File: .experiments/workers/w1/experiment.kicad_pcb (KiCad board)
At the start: 2 copper layers, 140 x 90 mm, 39 parts, among them J1 USB_C, J2 Output, J3 Debug, Q1 FS8205A, U1 USBLC6-2SC6, U2 BQ24072, U3 HY2113-KB5B, U4 MT3608, U5 AP2112K-3.3, U6 LN61CN3302MR-G

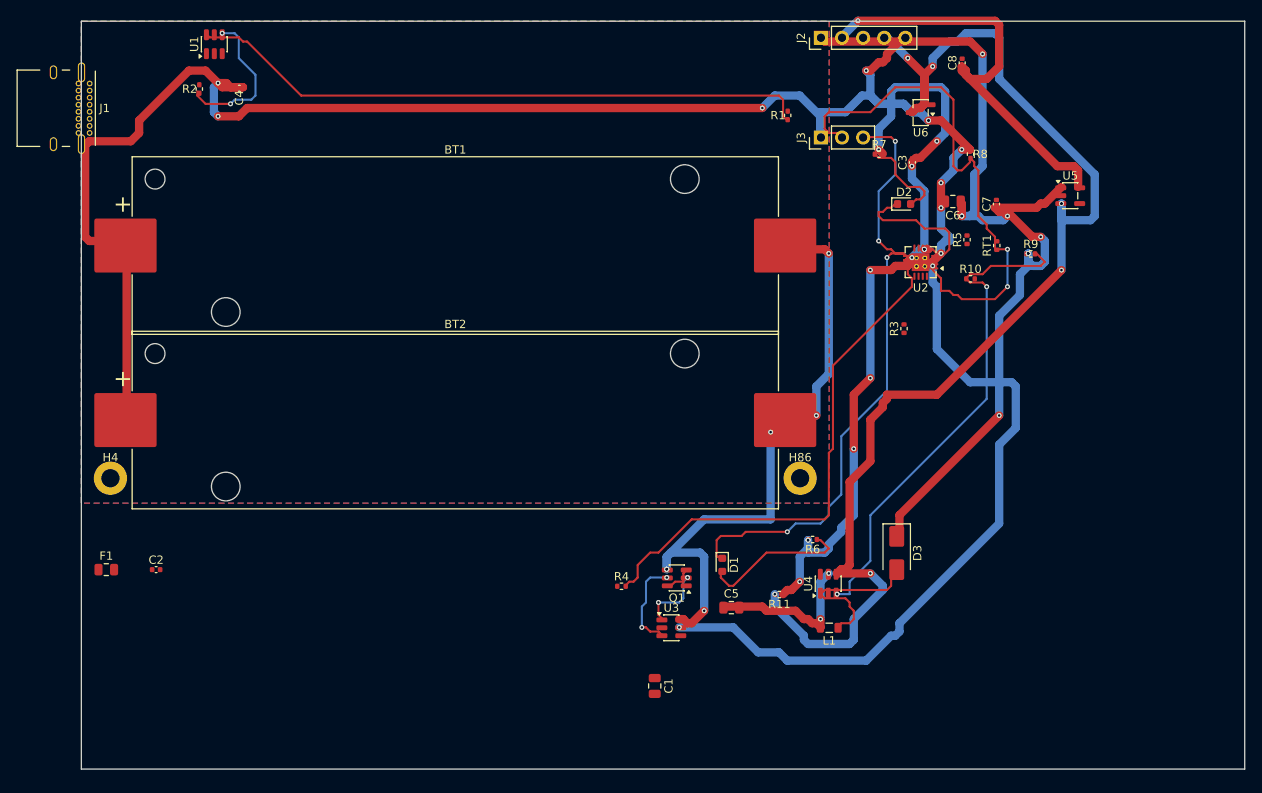
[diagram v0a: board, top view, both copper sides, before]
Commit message: 35-round experiment: best score 25.33, improved routing params
Router and conflict resolution tuning from autonomous optimization loop.
Best config: clearance=0.2051mm, cooling_factor=0.9735, existing_trace_cost=200.0

Co-Authored-By: Claude Opus 4.6 <noreply@anthropic.com>
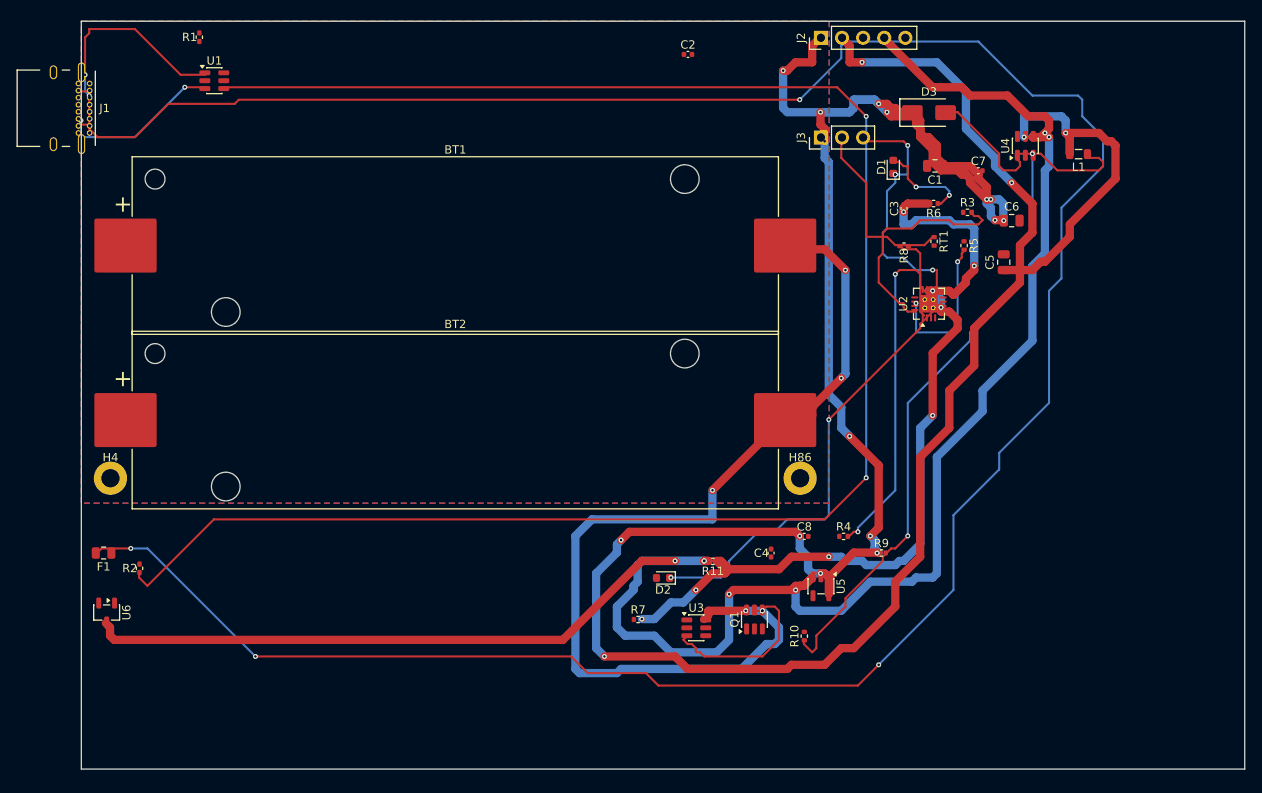
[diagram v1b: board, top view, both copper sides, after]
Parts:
- moved U6 115.0 mm to (3.04, 71.2), turned to -90 degrees
- moved C2 89.1 mm to (73.0, 4.00)
- moved C4 85.0 mm to (83.0, 64.0), turned to 90 degrees
- moved R1 71.4 mm to (14.2, 1.92)
- moved C1 71.1 mm to (102.7, 17.4), turned to 180 degrees
- moved L1 64.4 mm to (120.0, 16.0)
- moved R7 63.1 mm to (67.0, 72.0)
- moved C8 60.1 mm to (87.0, 62.0), turned to 0 degrees
- moved R2 58.1 mm to (7.00, 65.8)
- moved U4 57.8 mm to (113.6, 15.0)
- moved U5 55.8 mm to (89.0, 68.0), turned to -90 degrees
- moved D2 53.5 mm to (70.0, 67.0), turned to 180 degrees
- moved D3 53.1 mm to (102.0, 11.0), turned to 0 degrees
- moved C5 52.9 mm to (111.0, 29.0), turned to 90 degrees
- moved D1 52.1 mm to (97.7, 17.5), turned to 90 degrees
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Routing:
- net Net-(F1-Pad2): track 0.00 -> 317.3 mm, vias 0 -> 4
- net /VBAT: track 293.0 -> 0.00 mm, vias 14 -> 0
- net Net-(R2-Pad1): track 18.4 -> 216.2 mm
- net /3V3: track 52.5 -> 176.8 mm, vias 2 -> 6
- net /EN: track 149.0 -> 238.1 mm, vias 8 -> 6
- net Net-(R1-Pad1): track 75.5 -> 0.00 mm
- net /CHG_N: track 75.4 -> 30.9 mm
- net /CELL_NEG: track 75.5 -> 118.9 mm
- net Net-(D2-K): track 18.7 -> 53.8 mm, vias 0 -> 2
- net /5V: track 115.5 -> 146.3 mm, vias 8 -> 13
- net /NTC_SENSE: track 62.8 -> 32.7 mm, vias 2 -> 0
- net Net-(U2-ISET): track 0.00 -> 27.4 mm
- net Net-(J1-CC1): track 0.00 -> 24.7 mm, vias 0 -> 2
- net /VSYS_BOOST: track 19.4 -> 43.5 mm
- net Net-(U2-ILIM): track 62.7 -> 39.7 mm, vias 0 -> 2
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
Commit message: 45-round experiment: best score 25.66, all nets routed (26/26)
Fixed A* performance by increasing max_search from 100k->500k to handle
high trace costs (100.0) without timing out. Kept high cost + coarse grid
(0.5mm) to prevent shorts while still routing efficiently.

Best config: edge_margin=5.7493mm, cooling_factor=0.9764, existing_trace_cost=200, max_rips=8

Co-Authored-By: Claude Opus 4.6 <noreply@anthropic.com>
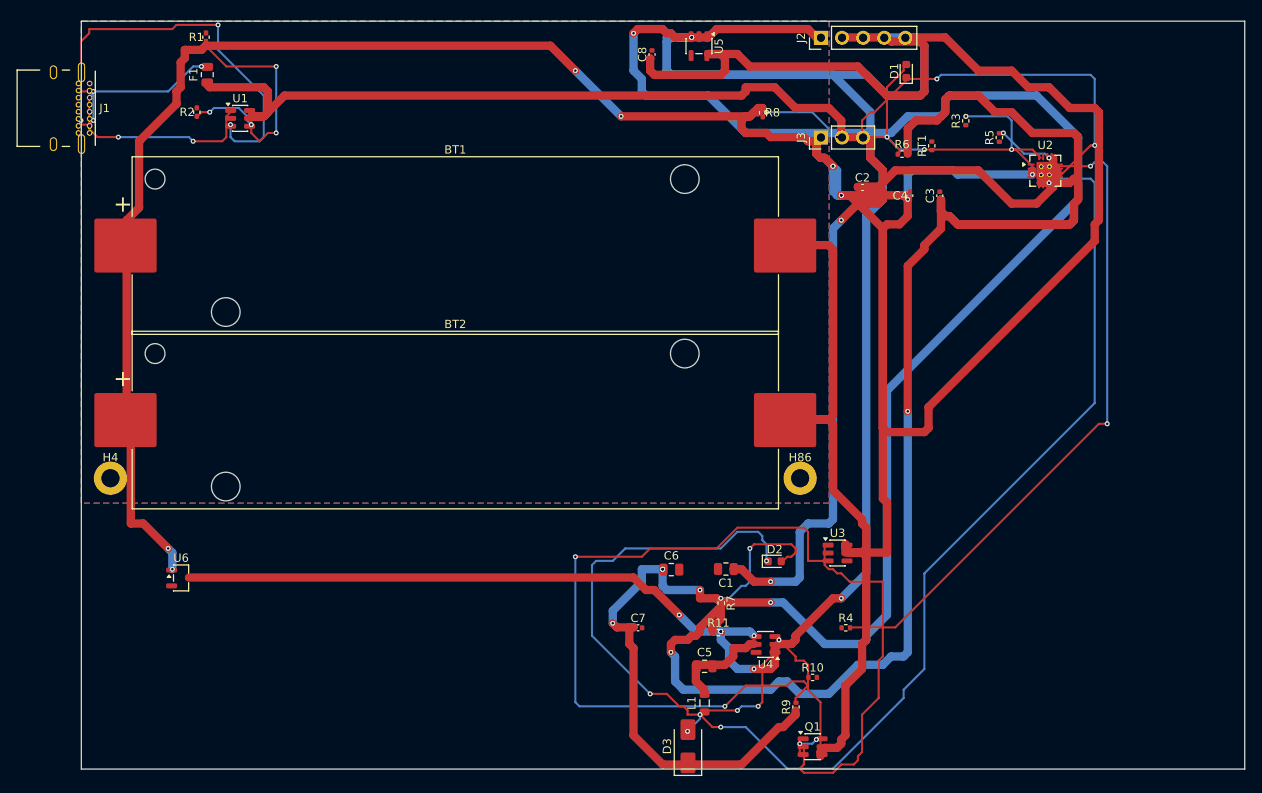
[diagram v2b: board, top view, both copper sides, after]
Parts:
- moved D3 81.6 mm to (73.0, 87.3), turned to 90 degrees
- moved L1 79.9 mm to (75.0, 82.1), turned to 90 degrees
- moved C7 68.6 mm to (67.0, 73.0)
- moved U4 67.7 mm to (82.3, 75.0), turned to 180 degrees
- moved U5 66.6 mm to (74.3, 3.00)
- moved C8 60.8 mm to (68.7, 4.00), turned to 90 degrees
- moved C5 60.5 mm to (75.0, 77.6), turned to 0 degrees
- moved F1 58.9 mm to (15.2, 6.43), turned to 90 degrees
- moved C6 58.7 mm to (71.0, 66.0)
- moved R2 55.3 mm to (13.9, 10.9)
- moved C1 54.7 mm to (77.6, 65.9)
- moved C4 46.1 mm to (99.7, 21.0)
- moved C2 26.4 mm to (94.0, 20.0)
- moved R8 23.4 mm to (82.0, 11.0), turned to -90 degrees
- moved U2 21.3 mm to (116.0, 18.0), turned to 0 degrees
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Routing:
- net /VBAT: track 0.00 -> 362.0 mm, vias 0 -> 10
- net Net-(F1-Pad2): track 317.3 -> 21.7 mm
- net Net-(R2-Pad1): track 216.2 -> 8.04 mm
- net /VBUS: track 0.00 -> 197.5 mm, vias 0 -> 2
- net /3V3: track 176.8 -> 58.8 mm, vias 6 -> 0
- net Net-(D2-K): track 53.8 -> 159.5 mm, vias 2 -> 4
- net /5V: track 146.3 -> 242.8 mm, vias 13 -> 7
- net /VSYS: track 103.1 -> 191.5 mm, vias 8 -> 2
- net Net-(Q1B-G): track 21.1 -> 90.9 mm, vias 0 -> 2
- net Net-(U4-FB): track 73.2 -> 10.9 mm, vias 2 -> 0
- net Net-(Q1A-G): track 0.00 -> 44.1 mm
- net Net-(U2-ILIM): track 39.7 -> 78.6 mm
- net /VSYS_BOOST: track 43.5 -> 12.5 mm, vias 2 -> 0
- net /CELL_NEG: track 118.9 -> 89.3 mm, vias 6 -> 0
- net Net-(J1-CC2): track 19.5 -> 48.8 mm, vias 2 -> 4
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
